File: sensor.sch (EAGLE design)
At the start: 17 parts, among them IC1 TINY261A

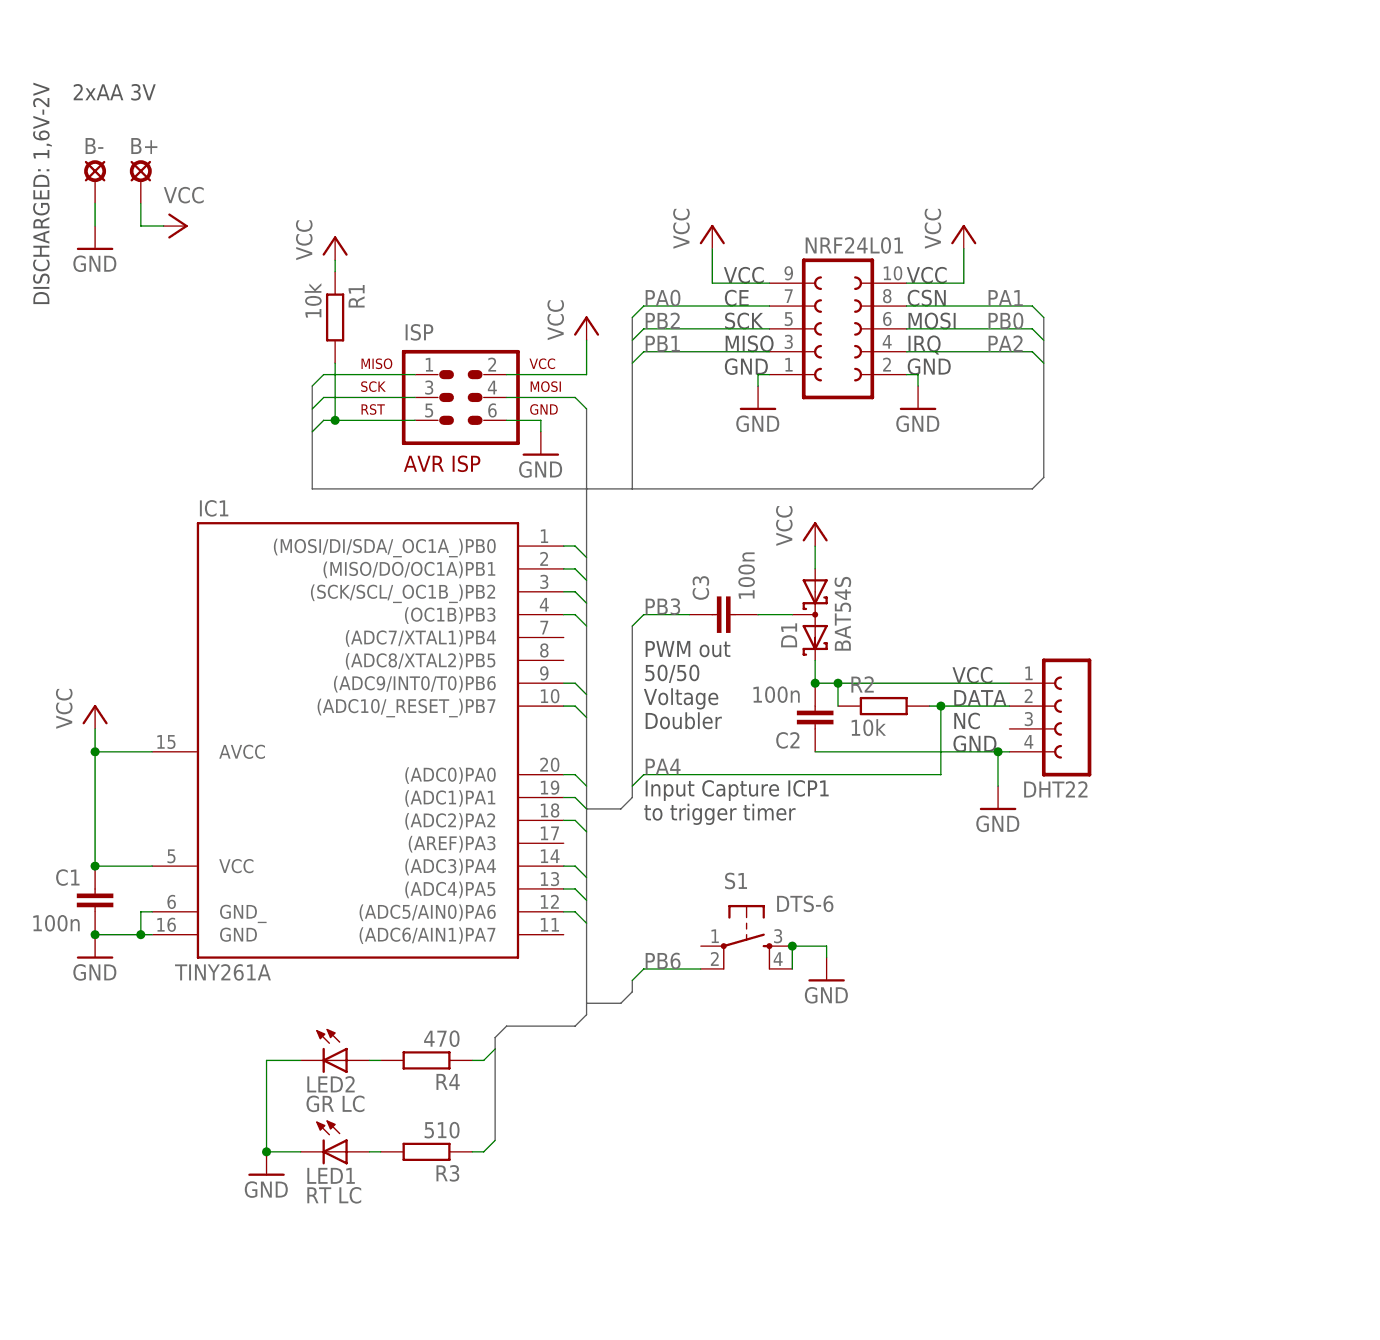
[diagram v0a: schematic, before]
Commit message: added watch crystal to master, notes for sensor
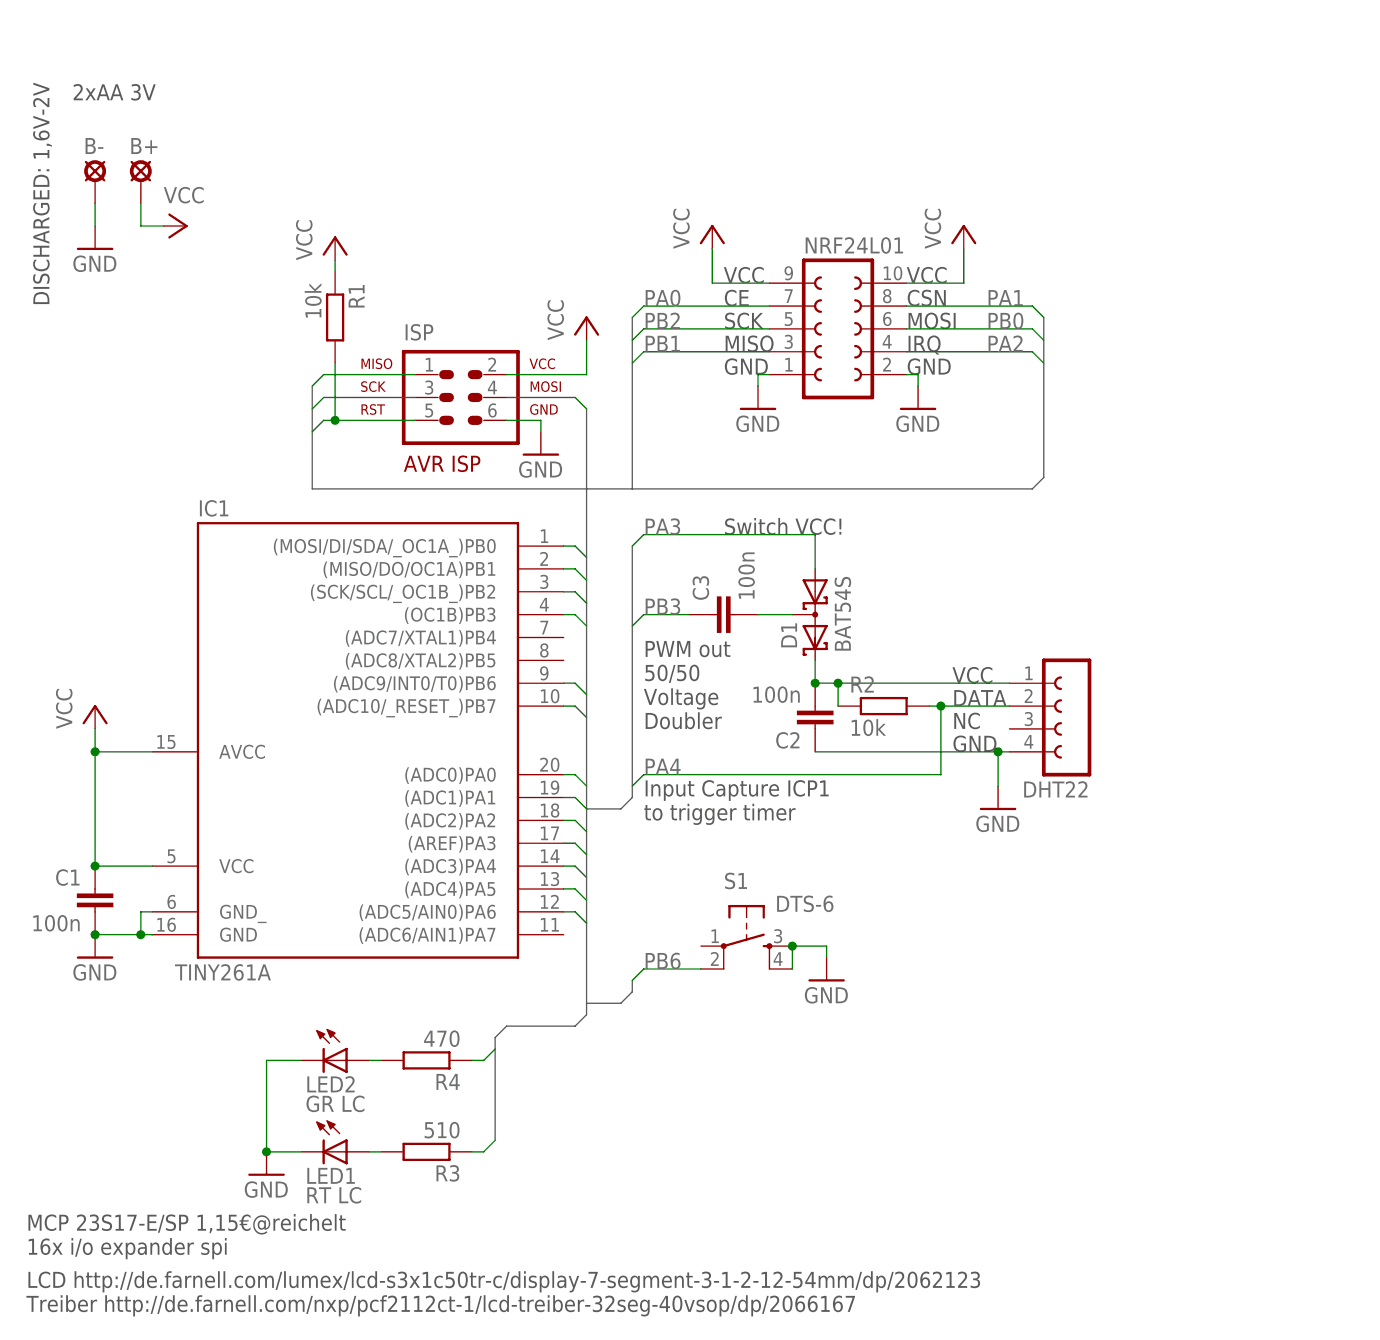
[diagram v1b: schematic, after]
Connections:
- new net PA3: D1.A1, IC1.(AREF)PA3
- net VCC: no longer D1.A1
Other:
- note added: "LCD http://de.farnell.com/lumex/lcd-s3x1c50tr-c/display-7-segment-3-1-2-12-54mm/dp/2062123 Treiber http://de.farnell.com/nxp/pcf2112ct-1/lcd-treiber-32seg-40vsop/dp/2066167"
- note added: "MCP 23S17-E/SP 1,15€@reichelt 16x i/o expander spi"
- note added: "Switch VCC!"
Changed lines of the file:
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@@
 <setting verticaltext="up"/>
 </settings>
-<grid distance="1.27" unitdist="mm" unit="mm" style="lines" multiple="1" display="yes" altdistance="635" altunitdist="mic" altunit="mic"/>
+<grid distance="0.1" unitdist="inch" unit="mm" style="lines" multiple="1" display="yes" altdistance="0.01" altunitdist="inch" altunit="mm"/>
 <layers>
-<layer number="1" name="Top" color="4" fill="1" visible="yes" active="no"/>
-<layer number="2" name="Route2" color="1" fill="3" visible="yes" active="no"/>
-<layer number="3" name="Route3" color="4" fill="3" visible="yes" active="no"/>
-<layer number="4" name="Route4" color="1" fill="4" visible="yes" active="no"/>
-<layer number="5" name="Route5" color="4" fill="4" visible="yes" active="no"/>
-<layer number="6" name="Route6" color="1" fill="8" visible="yes" active="no"/>
-<layer number="7" name="Route7" color="4" fill="8" visible="yes" active="no"/>
-<layer number="8" name="Route8" color="1" fill="2" visible="yes" active="no"/>
-<layer number="9" name="Route9" color="4" fill="2" visible="yes" active="no"/>
-<layer number="10" name="Route10" color="1" fill="7" visible="yes" active="no"/>
-<layer number="11" name="Route11" color="4" fill="7" visible="yes" active="no"/>
-<layer number="12" name="Route12" color="1" fill="5" visible="yes" active="no"/>
-<layer number="13" name="Route13" color="4" fill="5" visible="yes" active="no"/>
-<layer number="14" name="Route14" color="1" fill="6" visible="yes" active="no"/>
-<layer number="15" name="Route15" color="4" fill="6" visible="yes" active="no"/>
-<layer number="16" name="Bottom" color="1" fill="1" visible="yes" active="no"/>
-<layer number="17" name="Pads" color="2" fill="1" visible="yes" active="no"/>
-<layer number="18" name="Vias" color="2" fill="1" visible="yes" active="no"/>
-<layer number="19" name="Unrouted" color="6" fill="1" visible="yes" active="no"/>
-<layer number="20" name="Dimension" color="15" fill="1" visible="yes" active="no"/>
-<layer number="21" name="tPlace" color="7" fill="1" visible="yes" active="no"/>
-<layer number="22" name="bPlace" color="7" fill="1" visible="yes" active="no"/>
-<layer number="23" name="tOrigins" color="15" fill="1" visible="yes" active="no"/>
-<layer number="24" name="bOrigins" color="15" fill="1" visible="yes" active="no"/>
-<layer number="25" name="tNames" color="7" fill="1" visible="yes" active="no"/>
-<layer number="26" name="bNames" color="7" fill="1" visible="yes" active="no"/>
-<layer number="27" name="tValues" color="7" fill="1" visible="yes" active="no"/>
-<layer number="28" name="bValues" color="7" fill="1" visible="yes" active="no"/>
+<layer number="1" name="Top" color="4" fill="1" visible="no" active="no"/>
+<layer number="2" name="Route2" color="1" fill="3" visible="no" active="no"/>
+<layer number="3" name="Route3" color="4" fill="3" visible="no" active="no"/>
+<layer number="4" name="Route4" color="1" fill="4" visible="no" active="no"/>
+<layer number="5" name="Route5" color="4" fill="4" visible="no" active="no"/>
+<layer number="6" name="Route6" color="1" fill="8" visible="no" active="no"/>
+<layer number="7" name="Route7" color="4" fill="8" visible="no" active="no"/>
+<layer number="8" name="Route8" color="1" fill="2" visible="no" active="no"/>
+<layer number="9" name="Route9" color="4" fill="2" visible="no" active="no"/>
+<layer number="10" name="Route10" color="1" fill="7" visible="no" active="no"/>
+<layer number="11" name="Route11" color="4" fill="7" visible="no" active="no"/>
+<layer number="12" name="Route12" color="1" fill="5" visible="no" active="no"/>
+<layer number="13" name="Route13" color="4" fill="5" visible="no" active="no"/>
+<layer number="14" name="Route14" color="1" fill="6" visible="no" active="no"/>
+<layer number="15" name="Route15" color="4" fill="6" visible="no" active="no"/>
+<layer number="16" name="Bottom" color="1" fill="1" visible="no" active="no"/>
+<layer number="17" name="Pads" color="2" fill="1" visible="no" active="no"/>
+<layer number="18" name="Vias" color="2" fill="1" visible="no" active="no"/>
+<layer number="19" name="Unrouted" color="6" fill="1" visible="no" active="no"/>
+<layer number="20" name="Dimension" color="15" fill="1" visible="no" active="no"/>
+<layer number="21" name="tPlace" color="7" fill="1" visible="no" active="no"/>
+<layer number="22" name="bPlace" color="7" fill="1" visible="no" active="no"/>
+<layer number="23" name="tOrigins" color="15" fill="1" visible="no" active="no"/>
+<layer number="24" name="bOrigins" color="15" fill="1" visible="no" active="no"/>
+<layer number="25" name="tNames" color="7" fill="1" visible="no" active="no"/>
+<layer number="26" name="bNames" color="7" fill="1" visible="no" active="no"/>
+<layer number="27" name="tValues" color="7" fill="1" visible="no" active="no"/>
+<layer number="28" name="bValues" color="7" fill="1" visible="no" active="no"/>
 <layer number="29" name="tStop" color="7" fill="3" visible="no" active="no"/>
 <layer number="30" name="bStop" color="7" fill="6" visible="no" active="no"/>
@@
 <layer number="35" name="tGlue" color="7" fill="4" visible="no" active="no"/>
 <layer number="36" name="bGlue" color="7" fill="5" visible="no" active="no"/>
-<layer number="37" name="tTest" color="7" fill="1" visible="yes" active="no"/>
-<layer number="38" name="bTest" color="7" fill="1" visible="yes" active="no"/>
+<layer number="37" name="tTest" color="7" fill="1" visible="no" active="no"/>
+<layer number="38" name="bTest" color="7" fill="1" visible="no" active="no"/>
 <layer number="39" name="tKeepout" color="4" fill="11" visible="no" active="no"/>
 <layer number="40" name="bKeepout" color="1" fill="11" visible="no" active="no"/>
@@
 <layer number="44" name="Drills" color="7" fill="1" visible="no" active="no"/>
 <layer number="45" name="Holes" color="7" fill="1" visible="no" active="no"/>
-<layer number="46" name="Milling" color="3" fill="1" visible="yes" active="no"/>
-<layer number="47" name="Measures" color="7" fill="1" visible="yes" active="no"/>
-<layer number="48" name="Document" color="7" fill="1" visible="yes" active="no"/>
-<layer number="49" name="Reference" color="7" fill="1" visible="yes" active="no"/>
-<layer number="50" name="dxf" color="7" fill="1" visible="yes" active="no"/>
-<layer number="51" name="tDocu" color="7" fill="1" visible="yes" active="no"/>
-<layer number="52" name="bDocu" color="7" fill="1" visible="yes" active="no"/>
+<layer number="46" name="Milling" color="3" fill="1" visible="no" active="no"/>
+<layer number="47" name="Measures" color="7" fill="1" visible="no" active="no"/>
+<layer number="48" name="Document" color="7" fill="1" visible="no" active="no"/>
+<layer number="49" name="Reference" color="7" fill="1" visible="no" active="no"/>
+<layer number="50" name="dxf" color="7" fill="1" visible="no" active="no"/>
+<layer number="51" name="tDocu" color="7" fill="1" visible="no" active="no"/>
+<layer number="52" name="bDocu" color="7" fill="1" visible="no" active="no"/>
 <layer number="91" name="Nets" color="2" fill="1" visible="yes" active="yes"/>
 <layer number="92" name="Busses" color="1" fill="1" visible="yes" active="yes"/>
@@
 <part name="D1" library="diode" deviceset="BAT54S" device=""/>
 <part name="C3" library="rcl" deviceset="C-EU" device="C0805" value="100n"/>
-<part name="P+5" library="supply1" deviceset="VCC" device=""/>
 <part name="R3" library="rcl" deviceset="R-EU_" device="R0805" value="510"/>
 <part name="LED2" library="led" deviceset="LED" device="5MM" value="GR LC">
@@
 Voltage
 Doubler</text>
+<text x="82.55" y="118.11" size="1.778" layer="97">Switch VCC!</text>
+<text x="5.08" y="31.75" size="1.778" layer="97">LCD http://de.farnell.com/lumex/lcd-s3x1c50tr-c/display-7-segment-3-1-2-12-54mm/dp/2062123
+Treiber http://de.farnell.com/nxp/pcf2112ct-1/lcd-treiber-32seg-40vsop/dp/2066167</text>
+<text x="5.08" y="38.1" size="1.778" layer="97">MCP 23S17-E/SP 1,15€@reichelt
+16x i/o expander spi</text>
 </plain>
 <instances>
@@
 <instance part="D1" gate="G$1" x="92.71" y="109.22" rot="MR270"/>
 <instance part="C3" gate="G$1" x="81.28" y="109.22" rot="R90"/>
-<instance part="P+5" gate="VCC" x="92.71" y="119.38"/>
 <instance part="R3" gate="G$1" x="49.53" y="49.53" rot="R180"/>
 <instance part="LED2" gate="G$1" x="40.64" y="59.69" rot="R270">
@@
 <wire x1="67.31" y1="87.63" x2="71.12" y2="87.63" width="0.762" layer="92"/>
 <wire x1="71.12" y1="87.63" x2="72.39" y2="88.9" width="0.762" layer="92"/>
-<wire x1="72.39" y1="88.9" x2="72.39" y2="107.95" width="0.762" layer="92"/>
+<wire x1="72.39" y1="88.9" x2="72.39" y2="116.84" width="0.762" layer="92"/>
 <wire x1="67.31" y1="66.04" x2="67.31" y2="64.77" width="0.762" layer="92"/>
 <wire x1="67.31" y1="64.77" x2="66.04" y2="63.5" width="0.762" layer="92"/>
@@
 <pinref part="P+8" gate="VCC" pin="VCC"/>
 </segment>
-<segment>
-<pinref part="P+5" gate="VCC" pin="VCC"/>
-<pinref part="D1" gate="G$1" pin="A1"/>
-<wire x1="92.71" y1="114.3" x2="92.71" y2="116.84" width="0.1524" layer="91"/>
-</segment>
 </net>
 <net name="PA4" class="0">
@@
 </segment>
 </net>
+<net name="PA3" class="0">
+<segment>
+<pinref part="IC1" gate="G$1" pin="(AREF)PA3"/>
+<wire x1="64.77" y1="83.82" x2="66.04" y2="83.82" width="0.1524" layer="91"/>
+<wire x1="67.31" y1="82.55" x2="66.04" y2="83.82" width="0.1524" layer="91"/>
+</segment>
+<segment>
+<wire x1="72.39" y1="116.84" x2="73.66" y2="118.11" width="0.1524" layer="91"/>
+<wire x1="73.66" y1="118.11" x2="92.71" y2="118.11" width="0.1524" layer="91"/>
+<pinref part="D1" gate="G$1" pin="A1"/>
+<wire x1="92.71" y1="118.11" x2="92.71" y2="114.3" width="0.1524" layer="91"/>
+<label x="73.66" y="118.11" size="1.778" layer="95"/>
+</segment>
+</net>
 </nets>
 </sheet>
 </sheets>
-<errors>
-</errors>
 </schematic>
 </drawing>

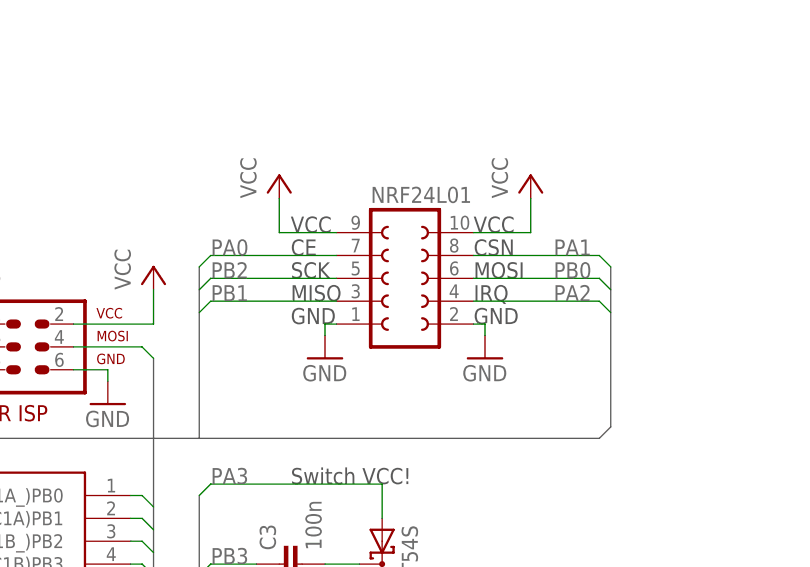
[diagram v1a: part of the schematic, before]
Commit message: di == miso, do == mosi for usi in spi mode
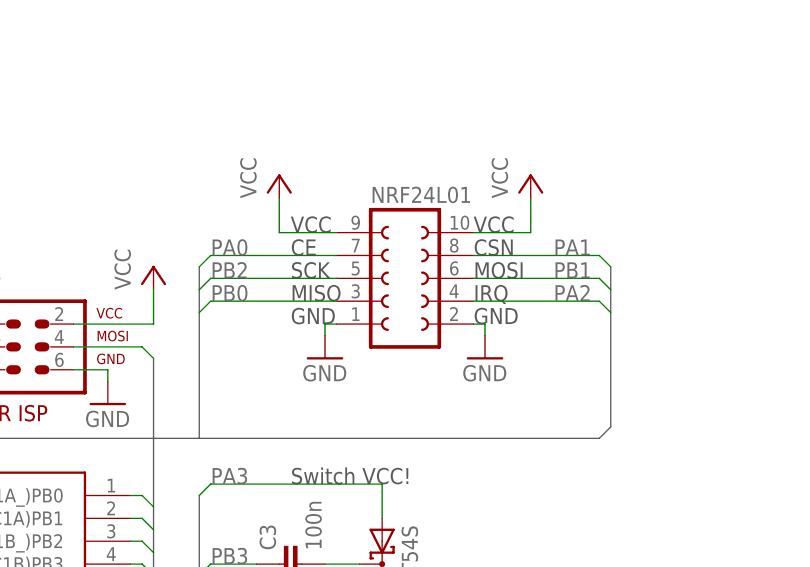
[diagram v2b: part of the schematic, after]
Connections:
- net PB0: now also NRF24L01.3; no longer NRF24L01.6
- net PB1: now also NRF24L01.6; no longer NRF24L01.3
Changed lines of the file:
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@@
 <setting verticaltext="up"/>
 </settings>
-<grid distance="0.1" unitdist="inch" unit="mm" style="lines" multiple="1" display="yes" altdistance="0.01" altunitdist="inch" altunit="mm"/>
+<grid distance="1.27" unitdist="mm" unit="mm" style="lines" multiple="1" display="yes" altdistance="635" altunitdist="mic" altunit="mic"/>
 <layers>
 <layer number="1" name="Top" color="4" fill="1" visible="no" active="no"/>
@@
 <net name="PB0" class="0">
 <segment>
-<pinref part="NRF24L01" gate="G$1" pin="6"/>
-<wire x1="116.84" y1="140.97" x2="118.11" y2="139.7" width="0.1524" layer="91"/>
-<wire x1="116.84" y1="140.97" x2="102.87" y2="140.97" width="0.1524" layer="91"/>
-<label x="111.76" y="140.97" size="1.778" layer="95"/>
-</segment>
-<segment>
 <wire x1="66.04" y1="133.35" x2="67.31" y2="132.08" width="0.1524" layer="91"/>
 <pinref part="ISP" gate="G$1" pin="4"/>
@@
 <wire x1="66.04" y1="116.84" x2="67.31" y2="115.57" width="0.1524" layer="91"/>
 </segment>
-</net>
-<net name="PB1" class="0">
 <segment>
 <pinref part="NRF24L01" gate="G$1" pin="3"/>
 <wire x1="87.63" y1="138.43" x2="73.66" y2="138.43" width="0.1524" layer="91"/>
-<wire x1="73.66" y1="138.43" x2="72.39" y2="137.16" width="0.1524" layer="91"/>
 <label x="73.66" y="138.43" size="1.778" layer="95"/>
-</segment>
+<wire x1="72.39" y1="137.16" x2="73.66" y2="138.43" width="0.1524" layer="91"/>
+</segment>
+</net>
+<net name="PB1" class="0">
 <segment>
 <pinref part="ISP" gate="G$1" pin="1"/>
@@
 <wire x1="66.04" y1="114.3" x2="67.31" y2="113.03" width="0.1524" layer="91"/>
 </segment>
-</net>
+<segment>
+<pinref part="NRF24L01" gate="G$1" pin="6"/>
+<wire x1="116.84" y1="140.97" x2="102.87" y2="140.97" width="0.1524" layer="91"/>
+<label x="111.76" y="140.97" size="1.778" layer="95"/>
+<wire x1="118.11" y1="139.7" x2="116.84" y2="140.97" width="0.1524" layer="91"/>
+</segment>
+</net>
